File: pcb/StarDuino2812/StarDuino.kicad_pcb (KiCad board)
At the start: 2 copper layers, 114.2 x 108.6 mm, 76 parts, among them J1 Screw_Terminal_01x02, J2 Conn_01x03_Male, Q1 IRLML6401, U1 ATmega328P-AU, Y1 16M

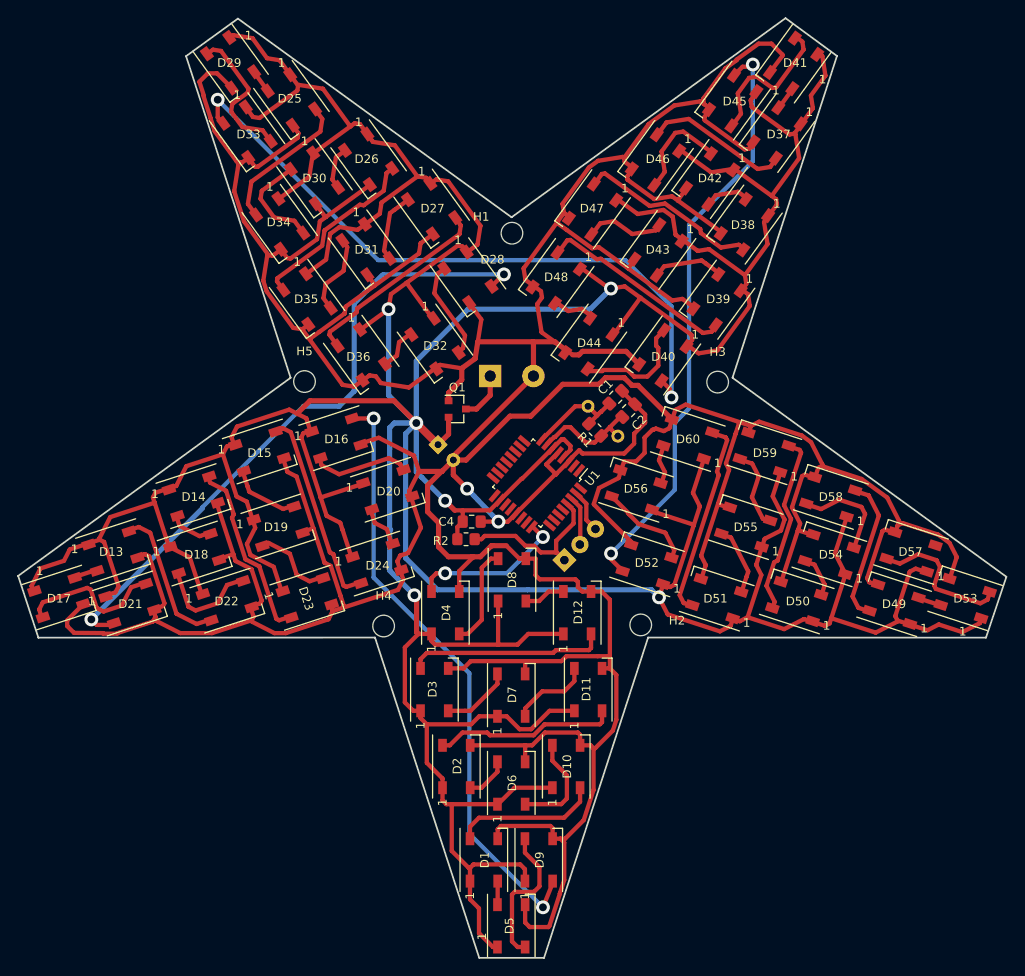
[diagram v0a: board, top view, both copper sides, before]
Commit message: Replace Mounting holes to Mounting pads Add capacitor Add resistors to UART
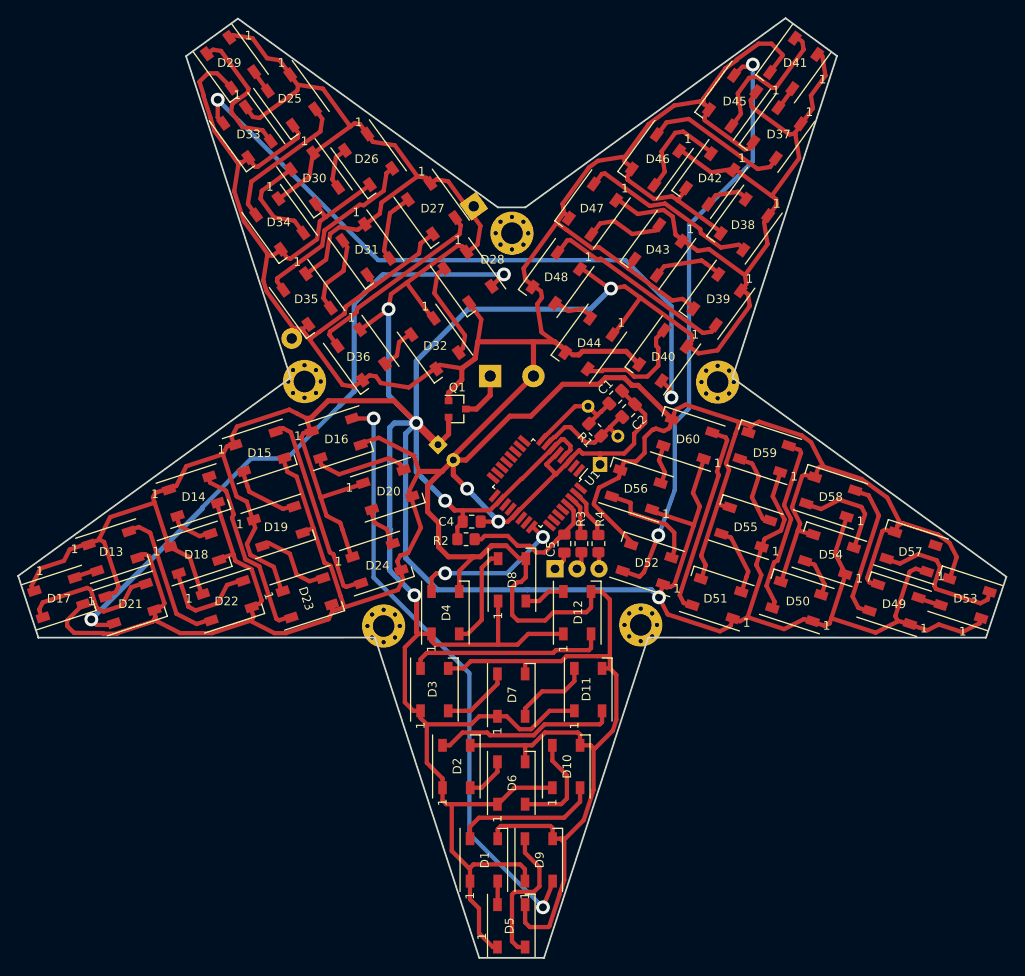
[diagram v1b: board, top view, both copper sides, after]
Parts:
- removed H1, H2, H3, H4, H5: MountingHole, MountingHole:MountingHole_2.5mm
- added C5: 0.1uF, Capacitor_SMD:C_0805_2012Metric_Pad1.18x1.45mm_HandSolder, F.Cu at (110.8, 101.6)
- added C6: 470uF, Capacitor_THT:CP_Axial_L20.0mm_D10.0mm_P26.00mm_Horizontal, B.Cu at (100.3, 62.6)
- added H10: MountingHole_Pad, MountingHole:MountingHole_2.5mm_Pad_Via, F.Cu at (80.8, 82.9)
- added H6: MountingHole_Pad, MountingHole:MountingHole_2.5mm_Pad_Via, F.Cu at (128.5, 82.9)
- added H7: MountingHole_Pad, MountingHole:MountingHole_2.5mm_Pad_Via, F.Cu at (119.6, 111.0)
- added H8: MountingHole_Pad, MountingHole:MountingHole_2.5mm_Pad_Via, F.Cu at (89.9, 111.1)
- added H9: MountingHole_Pad, MountingHole:MountingHole_2.5mm_Pad_Via, F.Cu at (104.7, 65.7)
- added J3: Conn_01x01_Male, Connector_PinHeader_2.54mm:PinHeader_1x01_P2.54mm_Vertical, B.Cu at (114.9, 92.5)
- added R3: 1k, Resistor_SMD:R_0805_2012Metric_Pad1.20x1.40mm_HandSolder, F.Cu at (112.8, 101.6)
- added R4: 1k, Resistor_SMD:R_0805_2012Metric_Pad1.20x1.40mm_HandSolder, F.Cu at (114.7, 101.6)
- moved J2 1.48 mm to (109.7, 104.5), turned to 270 degrees
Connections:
- J2 pad 1: /~Reset -> Net-(C5-Pad1)
- J2 pad 2: /RX -> Net-(J2-Pad2)
- J2 pad 3: /TX -> Net-(J2-Pad3)
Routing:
- net GND: track 718.4 -> 730.0 mm
- net Net-(C5-Pad1): track 0.00 -> 2.30 mm
- net Net-(J2-Pad2): track 0.00 -> 2.03 mm
- net Net-(J2-Pad3): track 0.00 -> 1.95 mm
- net Net-(D52-Pad2): track 11.0 -> 12.2 mm
- net /RX: track 5.71 -> 4.59 mm
- net /~Reset: track 18.4 -> 17.3 mm
- net /TX: track 5.02 -> 5.80 mm
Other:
- outline, holes or cut-outs redrawn

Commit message: Polishing. Add resistor, silk, etc
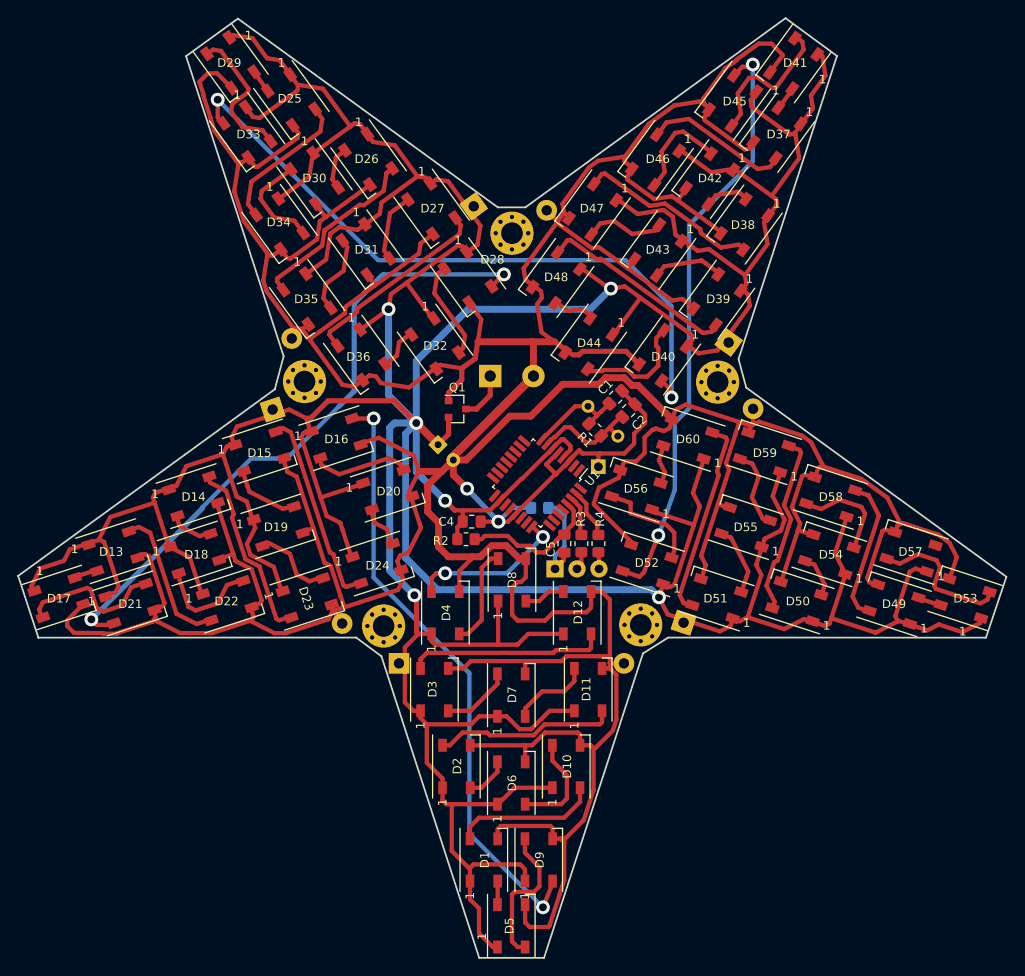
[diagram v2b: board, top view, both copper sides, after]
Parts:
- added C10: 470uF, Capacitor_THT:CP_Axial_L20.0mm_D10.0mm_P26.00mm_Horizontal, B.Cu at (91.7, 115.4)
- added C7: 470uF, Capacitor_THT:CP_Axial_L20.0mm_D10.0mm_P26.00mm_Horizontal, B.Cu at (124.6, 110.7)
- added C8: 470uF, Capacitor_THT:CP_Axial_L20.0mm_D10.0mm_P26.00mm_Horizontal, B.Cu at (129.8, 78.4)
- added C9: 470uF, Capacitor_THT:CP_Axial_L20.0mm_D10.0mm_P26.00mm_Horizontal, B.Cu at (77.1, 86.1)
- added R5: 1k, Resistor_SMD:R_0805_2012Metric_Pad1.20x1.40mm_HandSolder, B.Cu at (108.0, 97.5)
- moved J3 0.32 mm to (114.7, 92.7)
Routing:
- net GND: track 730.0 -> 741.9 mm
- net Net-(C5-Pad1): track 2.30 -> 11.1 mm
- net VCC: track 708.7 -> 711.0 mm
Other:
- outline, holes or cut-outs redrawn
- board text added: "+5V"
- board text added: "Gnd"
- board text added: "RX"
- board text added: "TX"
- board text added: "~Res"
